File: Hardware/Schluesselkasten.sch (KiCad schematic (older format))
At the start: 8 parts, among them J1 JACK_2P, SW1 SW_DPST_x2, U1 AP1117, U2 ESP-12F

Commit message: Added a few things
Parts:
- removed U1: AP1117, TO_SOT_Packages_SMD:SOT-223, symbol AP1117
- added D3: D, symbol D
- added J1, J2, J3, J4, J5, J6, J7, J8, J9: XLR3, symbol XLR3
- added JP1: Jumper_NC_Dual, symbol Jumper_NC_Dual
- added P?: Programmer_Breakout, symbol Programmer_Breakout
- added Q1: IRLR_7843, symbol IRLR_7843
- added R2, R4, R6: 12k, symbol R
- added R5, R8: 1k, symbol R
- added R7: 10k, symbol R
- added SW2: SW_Reed, symbol SW_Reed
- added Solenoid: L, symbol L
- added U1: Buck_Converter, symbol Buck_Converter
- added U3: CD74HC4067, symbol CD74HC4067
- added U5: RFID_Reader, symbol RFID_Reader
- renumbered J1 to J0
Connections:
- net labels added: +12V, GPIO_9, I_0, I_1, I_2, I_3, I_4, I_5, I_6, I_7, I_8, S_0, S_1, S_2, S_3
- net labels removed: +5V
- wire segments 25 -> 102
- no-connect marks 0 -> 16

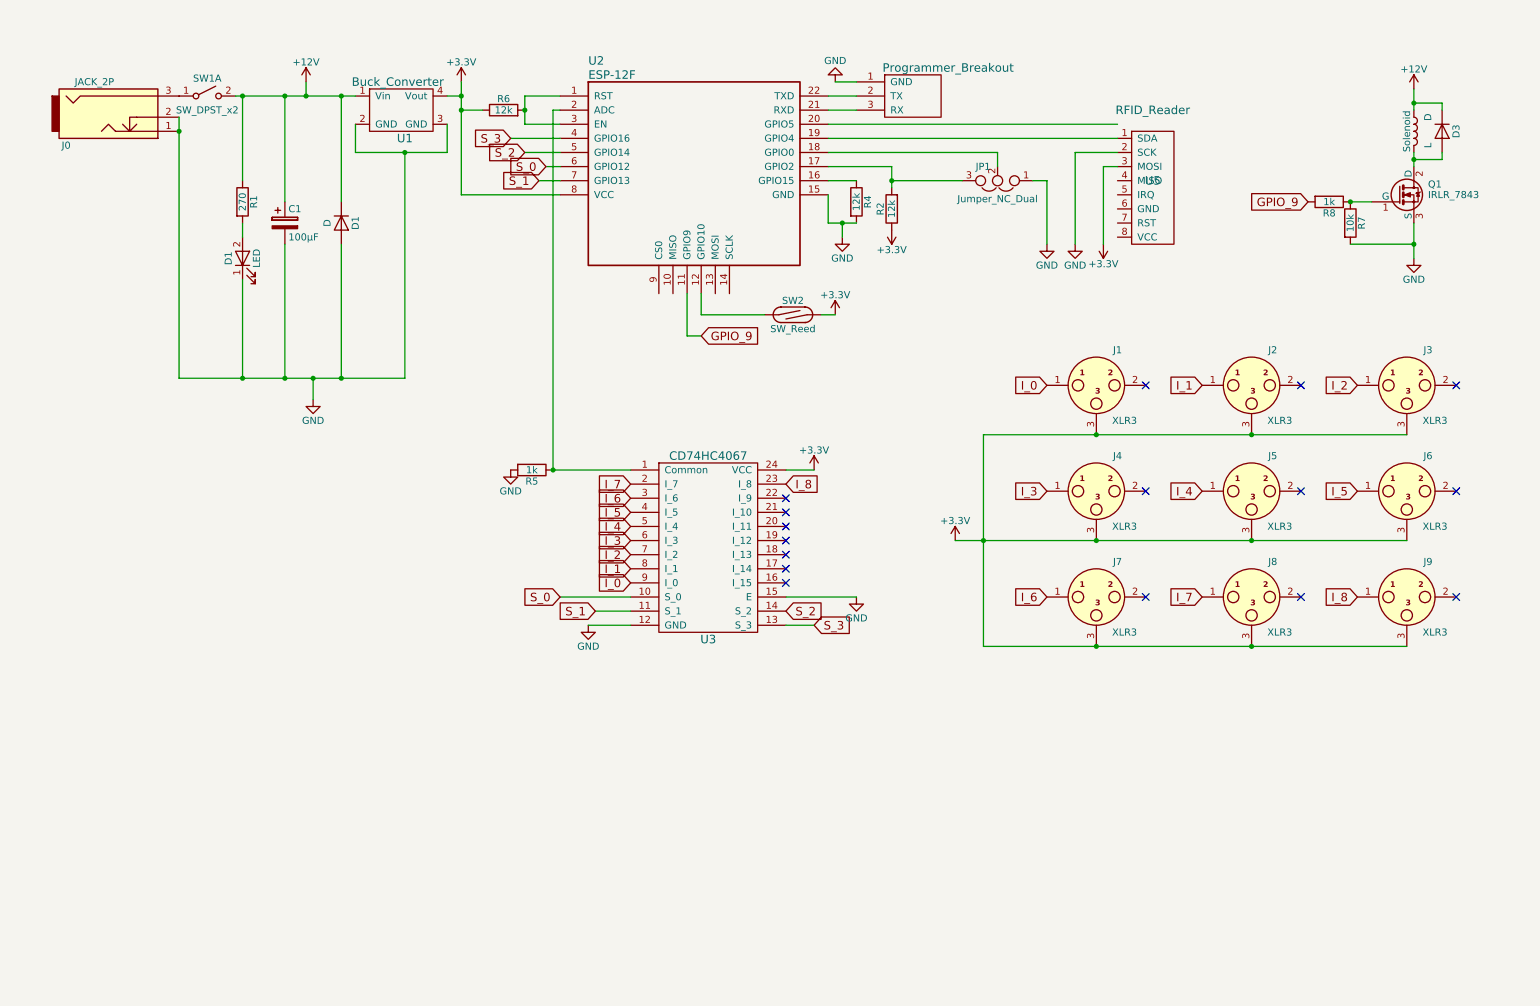
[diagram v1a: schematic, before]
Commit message: Changed the RFID-Reader to SPI
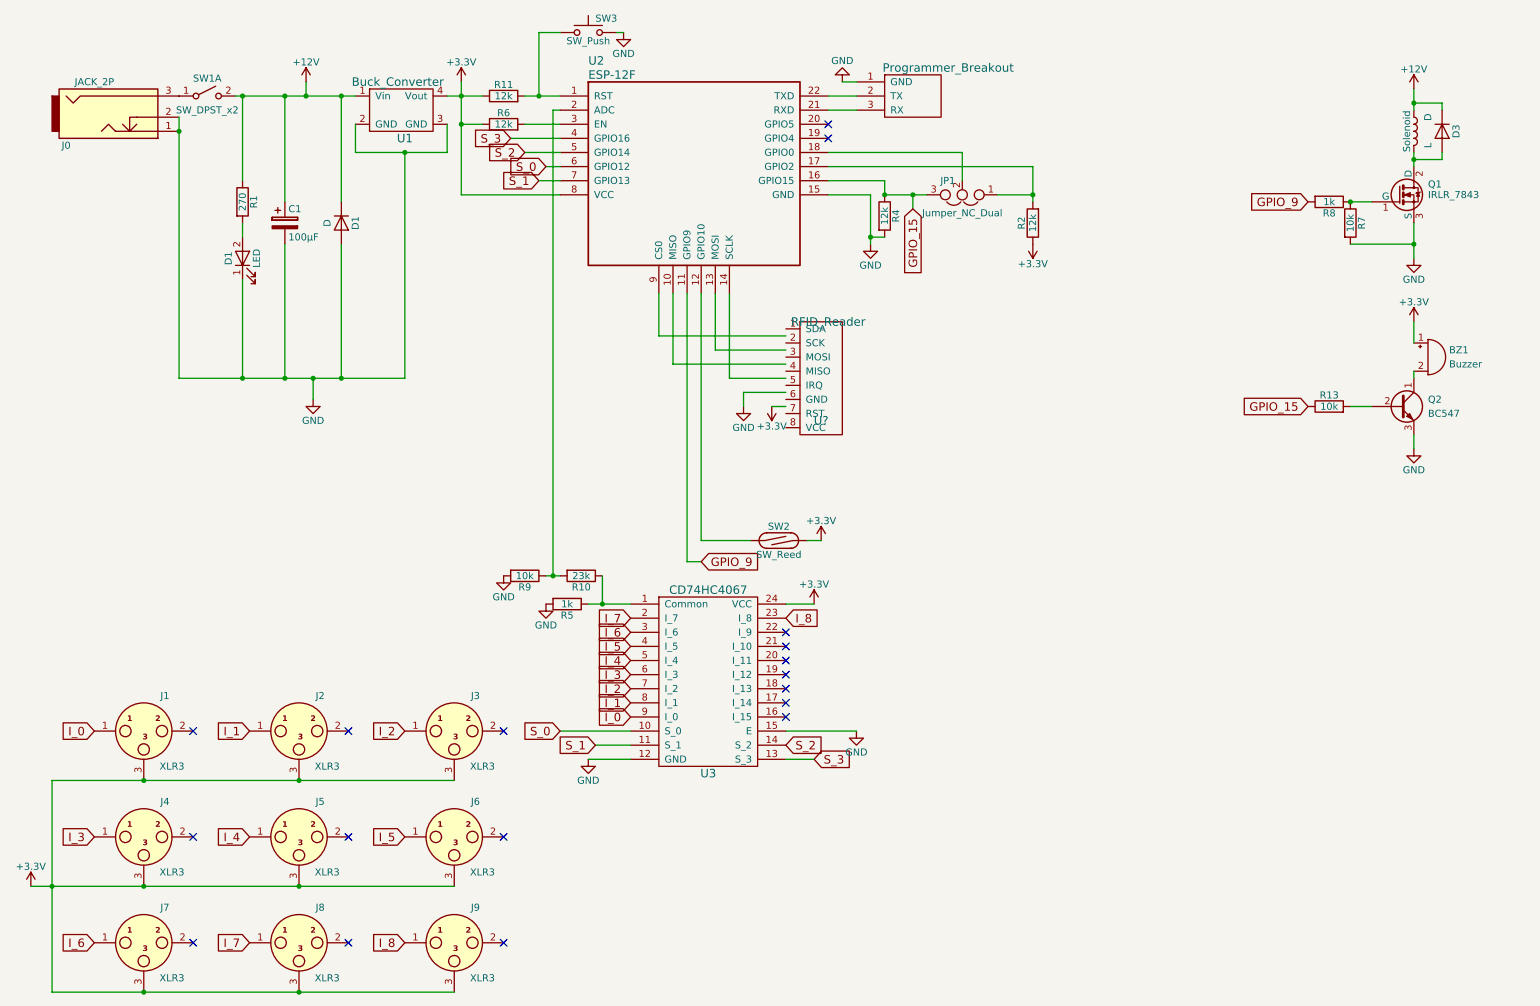
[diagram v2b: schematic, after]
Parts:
- removed U5: RFID_Reader, symbol RFID_Reader
- added BZ1: Buzzer, symbol Buzzer
- added Q2: BC547, symbol Q_NPN_CBE
- added R10: 23k, symbol R
- added R11: 12k, symbol R
- added R13, R9: 10k, symbol R
- added SW3: SW_Push, symbol SW_Push
- added U?: RFID_Reader, symbol RFID_Reader
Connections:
- net labels added: GPIO_15
- wire segments 102 -> 91
- no-connect marks 16 -> 18
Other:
- moved on the sheet: J1, J2, J3, J4, J5, J6, J7, J8, J9, JP1, R2, R4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

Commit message: Added a couple of things. I've been to lazy to upload them
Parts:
- added D?: R_LED, symbol LED
- added D?: G_LED, symbol LED
- added R?: 12k, symbol R
- added R?: 290, symbol R
- added R?: 270, symbol R
- added U?: 74HC595, symbol 74HC595
- R1: value 270 -> 670
- SW1: symbol SW_DPST_x2 -> SW_DPST_x2-RESCUE-Schluesselkasten
- SW2: symbol SW_Reed -> SW_Reed-RESCUE-Schluesselkasten
- gave numbers to parts that had none: 2
- renumbered D1 to D2, Solenoid to Solenoid1
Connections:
- net labels added: GPIO_0, GPIO_2, GPIO_4, GPIO_5
- net labels removed: GPIO_9
- wire segments 91 -> 116
- no-connect marks 18 -> 17
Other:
- note added: "Data Pin"
- note added: "Latch Pin"
- note added: "OE_ENABLE"
- note added: "Storage Reset"
- moved on the sheet: BZ1, D3, J3, JP1, Q1, Q2, R10, R11, R13, R2, R4, R5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

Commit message: Added a bunch of code
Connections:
- net GPIO_2: now also U?.11 (SRCLK); no longer U?.13 (G)
- net GPIO_4: now also U?.13 (G); no longer U?.14 (SER)
- net GPIO_5: now also U?.14 (SER); no longer U?.11 (SRCLK)
- net at SW2.1: now also R4.1, U2.16 (GPIO15); no longer U2.4 (GPIO16)
- net at R8.2: now also U?.5 (QF); no longer U?.4 (QE)
- net at R13.1: now also U?.4 (QE); no longer U?.5 (QF)
- removed net GPIO_15: R4.1, U2.16 (GPIO15), U4.1 (SDA)
- new net: U2.4 (GPIO16), U4.1 (SDA)
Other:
- moved on the sheet: BZ1, D3, Q1, Q2, R13, R7, R8, SW2, Solenoid1
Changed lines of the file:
@@
 L IRLR_7843 Q1
 U 1 1 598E6E65
-P 10650 1900
-F 0 "Q1" H 10850 1975 50  0000 L CNN
-F 1 "IRLR_7843" H 10850 1900 50  0000 L CNN
-F 2 "" H 10850 1825 50  0001 L CIN
-F 3 "" H 10650 1900 50  0001 L CNN
-	1    10650 1900
+P 10750 4050
+F 0 "Q1" H 10950 4125 50  0000 L CNN
+F 1 "IRLR_7843" H 10950 4050 50  0000 L CNN
+F 2 "" H 10950 3975 50  0001 L CIN
+F 3 "" H 10750 4050 50  0001 L CNN
+	1    10750 4050
 	1    0    0    -1
 $EndComp
@@
 L L Solenoid1
 U 1 1 598E716E
-P 10750 1450
-F 0 "Solenoid1" V 10700 1450 50  0000 C CNN
-F 1 "L" V 10850 1350 50  0000 C CNN
-F 2 "" H 10750 1450 50  0001 C CNN
-F 3 "" H 10750 1450 50  0001 C CNN
-	1    10750 1450
+P 10850 3600
+F 0 "Solenoid1" V 10800 3600 50  0000 C CNN
+F 1 "L" V 10950 3500 50  0000 C CNN
+F 2 "" H 10850 3600 50  0001 C CNN
+F 3 "" H 10850 3600 50  0001 C CNN
+	1    10850 3600
 	1    0    0    -1
 $EndComp
@@
 L D D3
 U 1 1 598E73CC
-P 10950 1450
-F 0 "D3" H 10950 1550 50  0000 C CNN
-F 1 "D" H 10850 1350 50  0000 C CNN
-F 2 "" H 10950 1450 50  0001 C CNN
-F 3 "" H 10950 1450 50  0001 C CNN
-	1    10950 1450
+P 11050 3600
+F 0 "D3" H 11050 3700 50  0000 C CNN
+F 1 "D" H 10950 3500 50  0000 C CNN
+F 2 "" H 11050 3600 50  0001 C CNN
+F 3 "" H 11050 3600 50  0001 C CNN
+	1    11050 3600
 	0    1    1    0
 $EndComp
@@
 L +12V #PWR09
 U 1 1 598E762B
-P 10750 1150
-F 0 "#PWR09" H 10750 1000 50  0001 C CNN
-F 1 "+12V" H 10750 1290 50  0000 C CNN
-F 2 "" H 10750 1150 50  0001 C CNN
-F 3 "" H 10750 1150 50  0001 C CNN
-	1    10750 1150
+P 10850 3300
+F 0 "#PWR09" H 10850 3150 50  0001 C CNN
+F 1 "+12V" H 10850 3440 50  0000 C CNN
+F 2 "" H 10850 3300 50  0001 C CNN
+F 3 "" H 10850 3300 50  0001 C CNN
+	1    10850 3300
 	1    0    0    -1
 $EndComp
@@
 L R R7
 U 1 1 598E77EB
-P 10400 2100
-F 0 "R7" V 10480 2100 50  0000 C CNN
-F 1 "10k" V 10400 2100 50  0000 C CNN
-F 2 "" V 10330 2100 50  0001 C CNN
-F 3 "" H 10400 2100 50  0001 C CNN
-	1    10400 2100
-	1    0    0    -1
-$EndComp
-$Comp
-L GND #PWR010
-U 1 1 598E7951
-P 10750 2350
-F 0 "#PWR010" H 10750 2100 50  0001 C CNN
-F 1 "GND" H 10750 2200 50  0000 C CNN
-F 2 "" H 10750 2350 50  0001 C CNN
-F 3 "" H 10750 2350 50  0001 C CNN
-	1    10750 2350
+P 10500 4250
+F 0 "R7" V 10580 4250 50  0000 C CNN
+F 1 "10k" V 10500 4250 50  0000 C CNN
+F 2 "" V 10430 4250 50  0001 C CNN
+F 3 "" H 10500 4250 50  0001 C CNN
+	1    10500 4250
 	1    0    0    -1
 $EndComp
@@
 L R R8
 U 1 1 598E7B97
-P 10250 1950
-F 0 "R8" V 10330 1950 50  0000 C CNN
-F 1 "1k" V 10250 1950 50  0000 C CNN
-F 2 "" V 10180 1950 50  0001 C CNN
-F 3 "" H 10250 1950 50  0001 C CNN
-	1    10250 1950
+P 10350 4100
+F 0 "R8" V 10430 4100 50  0000 C CNN
+F 1 "1k" V 10350 4100 50  0000 C CNN
+F 2 "" V 10280 4100 50  0001 C CNN
+F 3 "" H 10350 4100 50  0001 C CNN
+	1    10350 4100
 	0    1    1    0
 $EndComp
@@
 L SW_Reed-RESCUE-Schluesselkasten SW2
 U 1 1 598E8EA0
-P 4150 1700
-F 0 "SW2" H 4150 1800 50  0000 C CNN
-F 1 "SW_Reed" H 4150 1600 50  0000 C CNN
-F 2 "" H 4150 1700 50  0001 C CNN
-F 3 "" H 4150 1700 50  0001 C CNN
-	1    4150 1700
+P 7250 2000
+F 0 "SW2" H 7250 2100 50  0000 C CNN
+F 1 "SW_Reed" H 7250 1900 50  0000 C CNN
+F 2 "" H 7250 2000 50  0001 C CNN
+F 3 "" H 7250 2000 50  0001 C CNN
+	1    7250 2000
 	0    1    1    0
 $EndComp
@@
 L R R13
 U 1 1 598F6AB8
-P 10250 3400
-F 0 "R13" V 10330 3400 50  0000 C CNN
-F 1 "10k" V 10250 3400 50  0000 C CNN
-F 2 "" V 10180 3400 50  0001 C CNN
-F 3 "" H 10250 3400 50  0001 C CNN
-	1    10250 3400
+P 10350 2600
+F 0 "R13" V 10430 2600 50  0000 C CNN
+F 1 "10k" V 10350 2600 50  0000 C CNN
+F 2 "" V 10280 2600 50  0001 C CNN
+F 3 "" H 10350 2600 50  0001 C CNN
+	1    10350 2600
 	0    -1   -1   0
 $EndComp
@@
 L Q_NPN_CBE Q2
 U 1 1 598F70CC
-P 10650 3400
-F 0 "Q2" H 10850 3450 50  0000 L CNN
-F 1 "BC547" H 10850 3350 50  0000 L CNN
-F 2 "" H 10850 3500 50  0001 C CNN
-F 3 "" H 10650 3400 50  0001 C CNN
-	1    10650 3400
+P 10750 2600
+F 0 "Q2" H 10950 2650 50  0000 L CNN
+F 1 "BC547" H 10950 2550 50  0000 L CNN
+F 2 "" H 10950 2700 50  0001 C CNN
+F 3 "" H 10750 2600 50  0001 C CNN
+	1    10750 2600
 	1    0    0    -1
 $EndComp
@@
 L GND #PWR017
 U 1 1 598F837C
-P 10750 3700
-F 0 "#PWR017" H 10750 3450 50  0001 C CNN
-F 1 "GND" H 10750 3550 50  0000 C CNN
-F 2 "" H 10750 3700 50  0001 C CNN
-F 3 "" H 10750 3700 50  0001 C CNN
-	1    10750 3700
+P 10850 2900
+F 0 "#PWR017" H 10850 2650 50  0001 C CNN
+F 1 "GND" H 10850 2750 50  0000 C CNN
+F 2 "" H 10850 2900 50  0001 C CNN
+F 3 "" H 10850 2900 50  0001 C CNN
+	1    10850 2900
 	1    0    0    -1
 $EndComp
@@
 L Buzzer BZ1
 U 1 1 598F84E2
-P 10850 3050
-F 0 "BZ1" H 11000 3100 50  0000 L CNN
-F 1 "Buzzer" H 11000 3000 50  0000 L CNN
-F 2 "" V 10825 3150 50  0001 C CNN
-F 3 "" V 10825 3150 50  0001 C CNN
-	1    10850 3050
+P 10950 2250
+F 0 "BZ1" H 11100 2300 50  0000 L CNN
+F 1 "Buzzer" H 11100 2200 50  0000 L CNN
+F 2 "" V 10925 2350 50  0001 C CNN
+F 3 "" V 10925 2350 50  0001 C CNN
+	1    10950 2250
 	1    0    0    -1
 $EndComp
@@
 L +3.3V #PWR018
 U 1 1 5990658A
-P 10750 2800
-F 0 "#PWR018" H 10750 2650 50  0001 C CNN
-F 1 "+3.3V" H 10750 2940 50  0000 C CNN
-F 2 "" H 10750 2800 50  0001 C CNN
-F 3 "" H 10750 2800 50  0001 C CNN
-	1    10750 2800
+P 10850 2000
+F 0 "#PWR018" H 10850 1850 50  0001 C CNN
+F 1 "+3.3V" H 10850 2140 50  0000 C CNN
+F 2 "" H 10850 2000 50  0001 C CNN
+F 3 "" H 10850 2000 50  0001 C CNN
+	1    10850 2000
 	1    0    0    -1
 $EndComp
@@
 Wire Wire Line
 	2750 1200 2750 1100
-Connection ~ 10400 1950
-Connection ~ 10750 2250
-Wire Wire Line
-	10750 2100 10750 2350
-Wire Wire Line
-	10400 2250 10750 2250
-Wire Wire Line
-	10400 1950 10450 1950
-Connection ~ 10750 1250
-Connection ~ 10750 1650
-Wire Wire Line
-	10950 1650 10950 1600
-Wire Wire Line
-	10750 1650 10950 1650
-Wire Wire Line
-	10750 1600 10750 1700
-Wire Wire Line
-	10750 1150 10750 1300
-Wire Wire Line
-	10950 1250 10750 1250
-Wire Wire Line
-	10950 1300 10950 1250
+Connection ~ 10500 4100
+Connection ~ 10850 4400
+Wire Wire Line
+	10850 4250 10850 4600
+Wire Wire Line
+	10500 4400 10850 4400
+Wire Wire Line
+	10500 4100 10550 4100
+Connection ~ 10850 3400
+Connection ~ 10850 3800
+Wire Wire Line
+	11050 3800 11050 3750
+Wire Wire Line
+	10850 3800 11050 3800
+Wire Wire Line
+	10850 3750 10850 3850
+Wire Wire Line
+	10850 3300 10850 3450
+Wire Wire Line
+	11050 3400 10850 3400
+Wire Wire Line
+	11050 3450 11050 3400
 Connection ~ 950  6800
 Connection ~ 1600 6800
@@
 	7000 1850 7000 1800
 Wire Wire Line
-	6600 1800 7050 1800
+	6600 1800 7250 1800
 Wire Wire Line
 	6900 1900 6900 2350
@@
 Connection ~ 6900 2200
 Wire Wire Line
-	10750 3700 10750 3600
-Wire Wire Line
-	10750 3150 10750 3200
-Wire Wire Line
-	10400 3400 10450 3400
-Wire Wire Line
-	10100 3400 10000 3400
-Wire Wire Line
-	10750 2800 10750 2950
+	10850 2900 10850 2800
+Wire Wire Line
+	10850 2350 10850 2400
+Wire Wire Line
+	10500 2600 10550 2600
+Wire Wire Line
+	9900 2600 10200 2600
+Wire Wire Line
+	10850 2000 10850 2150
 Wire Wire Line
 	5050 3650 5700 3650
@@
 	4500 1800 4700 1800
 Wire Wire Line
-	5700 2950 5650 2950
-Wire Wire Line
-	4150 1500 4700 1500
-Connection ~ 4150 1900
+	4200 2950 5700 2950
 Wire Wire Line
 	6600 1600 7650 1600
@@
 	9600 4200 8800 4200
 Wire Wire Line
-	9900 1950 10100 1950
-Wire Wire Line
-	9900 1950 9900 4300
-Wire Wire Line
-	9900 4300 8800 4300
-Wire Wire Line
-	10000 3400 10000 4400
-Wire Wire Line
-	10000 4400 8800 4400
+	10000 4100 10200 4100
 Wire Wire Line
 	8300 5000 8300 5050
@@
 $EndComp
 Wire Wire Line
-	10700 4600 10850 4600
-Wire Wire Line
-	10850 4600 10850 4500
+	10850 4600 10700 4600
 Wire Wire Line
 	10850 4500 10350 4500
@@
 GPIO_2
 Connection ~ 8050 1700
-Text GLabel 7750 4500 0    60   Input ~ 0
+Text GLabel 7350 4100 0    60   Input ~ 0
 GPIO_2
 Wire Wire Line
@@
 Text GLabel 7350 4400 0    60   Input ~ 0
 GPIO_0
+Text GLabel 7750 4500 0    60   Input ~ 0
+GPIO_4
 Text GLabel 7350 3900 0    60   Input ~ 0
-GPIO_4
-Text GLabel 7350 4100 0    60   Input ~ 0
 GPIO_5
 Wire Wire Line
@@
 Text Notes 6550 3950 0    60   ~ 0
 Data Pin
-Text GLabel 7050 1800 2    60   Input ~ 0
-GPIO_15
 Connection ~ 7000 1800
-Text GLabel 5650 2950 0    60   Input ~ 0
-GPIO_15
 Text GLabel 6550 5700 2    60   Input ~ 0
 GPIO_2
@@
 	7000 2200 7000 2150
 NoConn ~ 5700 3350
+Wire Wire Line
+	4200 2950 4200 1500
+Wire Wire Line
+	4200 1500 4700 1500
+$Comp
+L +3.3V #PWR?
+U 1 1 59CE6639
+P 7250 2350
+F 0 "#PWR?" H 7250 2200 50  0001 C CNN
+F 1 "+3.3V" H 7250 2490 50  0000 C CNN
+F 2 "" H 7250 2350 50  0001 C CNN
+F 3 "" H 7250 2350 50  0001 C CNN
+	1    7250 2350
+	-1   0    0    1
+$EndComp
+Wire Wire Line
+	7250 2350 7250 2200
+Wire Wire Line
+	9900 4300 8800 4300
+Wire Wire Line
+	10000 4400 8800 4400
+Connection ~ 10850 4500
+Wire Wire Line
+	10000 4400 10000 4100
+Wire Wire Line
+	9900 4300 9900 2600
 $EndSCHEMATC
